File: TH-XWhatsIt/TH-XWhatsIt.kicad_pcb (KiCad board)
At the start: 2 copper layers, 162.2 x 18.8 mm, 27 parts, among them J1 BEAMSPRING CONNECTOR, J3 EXPANSION HEADER, U1 MCP4921-EP, U2 LM339, U3 74HCT595, U4 74HCT595, U5 ProMicro, U7 74HCT595

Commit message: added lcsc numbers for remaining chips, changed some silkscreen to match parts, removed stay-upright flag from all silkscreen, etc...
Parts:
- U1: value MCP4921-EP -> MCP4921-E
- U2: value LM339 -> LM339A
- U3, U4, U7: value 74HCT595 -> 74AHC595

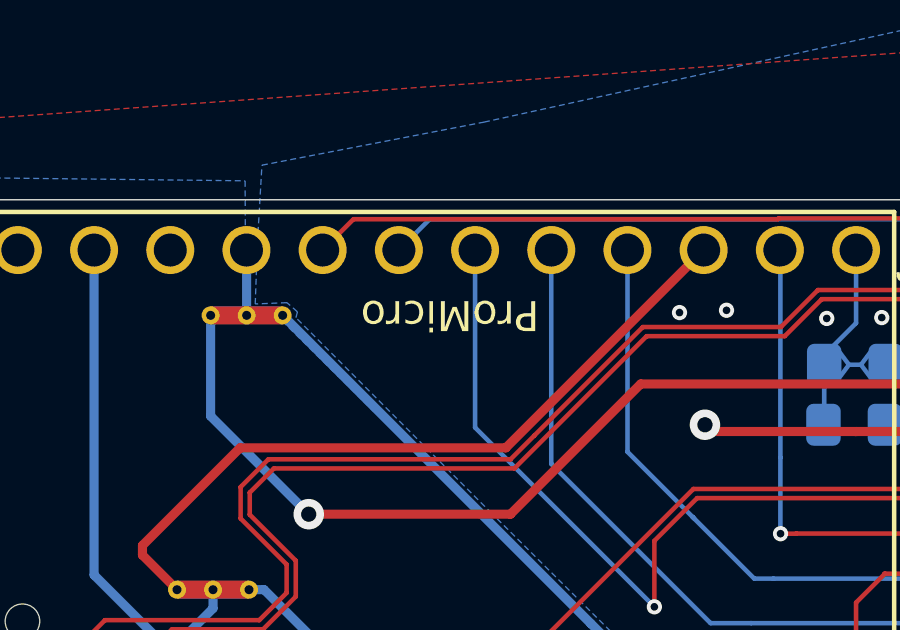
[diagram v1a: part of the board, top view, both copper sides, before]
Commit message: rotated pro micro silkscreen
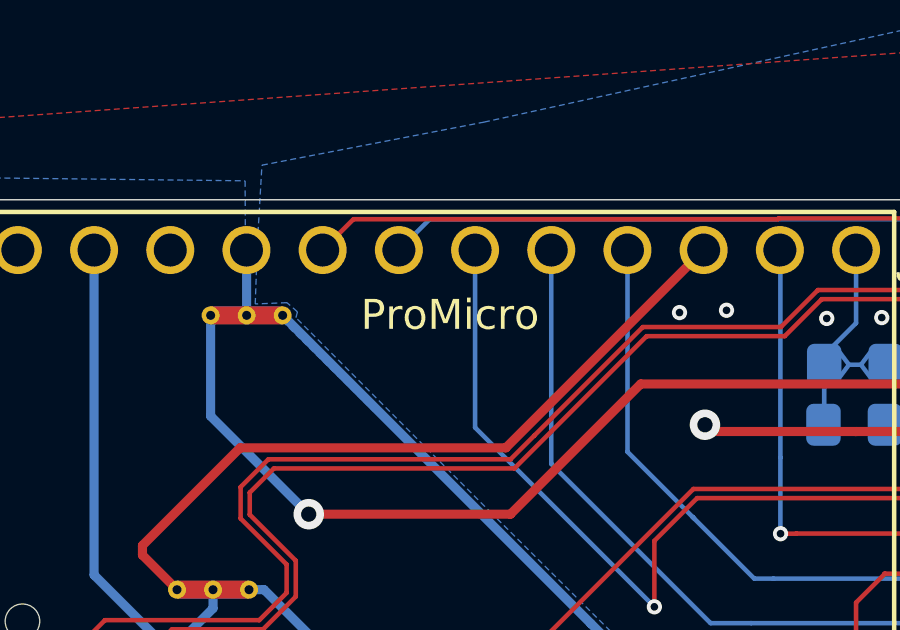
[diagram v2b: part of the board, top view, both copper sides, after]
